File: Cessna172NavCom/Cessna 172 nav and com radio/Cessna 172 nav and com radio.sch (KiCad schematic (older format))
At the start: 19 parts, among them J1 Board connector, U1 MAX7219 COM standby, U2 COM active 4, U3 COM active 4, U4 COM active 4, U5 COM active 4, U6 COM active 4

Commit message: Minor update
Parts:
- removed R?: 27k, symbol Device:R
- removed U3, U4, U5, U6: COM active 4, Display_7Segment:KCSC02-105, symbol Display_Character:KCSC02-105
- removed U?: MAX7219 COM standby, symbol Driver_LED:MAX7219
- removed U?: COM standby 4, Display_7Segment:KCSC02-105, symbol Display_Character:KCSC02-105
- removed U?: COM standby 3, Display_7Segment:KCSC02-105, symbol Display_Character:KCSC02-105
- removed U?: COM standby 2, Display_7Segment:KCSC02-105, symbol Display_Character:KCSC02-105
- removed U?: COM standby 1, Display_7Segment:KCSC02-105, symbol Display_Character:KCSC02-105
- removed U?: COM standby 0, Display_7Segment:KCSC02-105, symbol Display_Character:KCSC02-105
- added LED2, LED3, LED4, LED5: Mobiflight digit 5, Display_7Segment:KCSC02-105, symbol Display_Character:KCSC02-105
- LED1: renamed from U2; value COM active 4 -> Mobiflight digit 5
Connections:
- net labels added: MAX0, MAX1, MAX10, MAX11, MAX12, MAX13, MAX2, MAX3, MAX4, MAX5, MAX6, MAX7, MAX9
- net labels removed: COMA_0, COMA_1, COMA_2, COMA_3, COMA_4, COMA_A, COMA_B, COMA_C, COMA_D, COMA_DP, COMA_E, COMA_F, COMA_G, COMS_0, COMS_1, COMS_2, COMS_3, COMS_4, COMS_A, COMS_B, COMS_C, COMS_D, COMS_DP, COMS_E, COMS_F, COMS_G
- wire segments 22 -> 76
- no-connect marks 17 -> 9
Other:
- note added: "5 segment display"
- note removed: "COM1 active frequency display"
- note removed: "COM1 standby frequency display"
- moved on the sheet: LED1, R1, U1

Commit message: Five digit displays wired up
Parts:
- removed LED1, LED2, LED3, LED4, LED5: Mobiflight digit 5, Display_7Segment:KCSC02-105, symbol Display_Character:KCSC02-105
- removed R1: 27k, symbol Device:R
- removed U1: MAX7219 COM standby, symbol Driver_LED:MAX7219
- C1: value C -> 10uF; footprint (none) -> Capacitor_THT:CP_Radial_D5.0mm_P2.00mm
- C2, C3, C4: value C -> 0.1uF; footprint (none) -> Capacitor_THT:C_Disc_D3.0mm_W2.0mm_P2.50mm
- J1: footprint (none) -> Connector_PinHeader_2.54mm:PinHeader_1x06_P2.54mm_Vertical
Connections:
- net labels removed: MAX0, MAX1, MAX10, MAX11, MAX12, MAX13, MAX2, MAX3, MAX4, MAX5, MAX6, MAX7, MAX9
- wire segments 76 -> 37
- no-connect marks 9 -> 2
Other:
- note added: "COMM active"
- note added: "COMM standby"
- note added: "LCD displays"
- note added: "NAV active"
- note added: "NAV standby"
- note removed: "5 segment display"

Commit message: Add rotary encoder
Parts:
- removed J1: Board connector, Connector_PinHeader_2.54mm:PinHeader_1x06_P2.54mm_Vertical, symbol Connector_Generic:Conn_02x03_Counter_Clockwise
- added C5, C6: 0.1uf, symbol Device:C
- added J1: Conn_02x08_Counter_Clockwise, symbol Connector_Generic:Conn_02x08_Counter_Clockwise
- added R5, R6, R7, R8: 10k, Resistor_SMD:R_0805_2012Metric_Pad1.15x1.40mm_HandSolder, symbol Device:R
- added SW1: Tuning encoder, Rotary_Encoder:RotaryEncoder_Alps_EC11E-Switch_Vertical_H20mm, symbol Device:Rotary_Encoder_Switch
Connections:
- net labels added: R_LEFT, R_RIGHT, SW
- wire segments 37 -> 50
- no-connect marks 2 -> 9
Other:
- note added: "Tuning rotary encoder and switch"
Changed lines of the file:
@@
 Comment4 ""
 $EndDescr
-Text GLabel 1400 1750 2    50   Input ~ 0
+Text GLabel 1400 1750 2    50   Output ~ 0
 LOAD
-Text GLabel 1400 1850 2    50   Input ~ 0
+Text GLabel 1400 1850 2    50   Output ~ 0
 CLK
-Text GLabel 1400 1950 2    50   Input ~ 0
+Text GLabel 1400 1950 2    50   Output ~ 0
 DIN
 $Comp
@@
 Wire Wire Line
 	2200 1200 2350 1200
-Text GLabel 2550 1050 2    50   Input ~ 0
+Text GLabel 2550 1050 2    50   Output ~ 0
 +5V
-Text GLabel 2550 1150 2    50   Input ~ 0
+Text GLabel 2550 1150 2    50   Output ~ 0
 GND
 $Comp
@@
 Wire Wire Line
 	2350 1200 2500 1200
-$Comp
-L Connector_Generic:Conn_02x03_Counter_Clockwise J1
-U 1 1 5F5EC70C
-P 1100 1850
-F 0 "J1" H 1150 2167 50  0000 C CNN
-F 1 "Board connector" H 1150 2076 50  0000 C CNN
-F 2 "Connector_PinHeader_2.54mm:PinHeader_1x06_P2.54mm_Vertical" H 1100 1850 50  0001 C CNN
-F 3 "~" H 1100 1850 50  0001 C CNN
-	1    1100 1850
-	1    0    0    -1
-$EndComp
-Connection ~ 900  1750
 NoConn ~ 900  1950
-Wire Notes Line
-	550  2050 2800 2050
 Wire Notes Line
 	2800 2050 2800 650
@@
 Text Notes 3200 600  0    50   ~ 0
 LCD displays
+$Comp
+L Device:Rotary_Encoder_Switch SW1
+U 1 1 5F5CDBEE
+P 4500 3550
+F 0 "SW1" H 4750 3250 50  0000 L CNN
+F 1 "Tuning encoder" H 4750 3350 50  0000 L CNN
+F 2 "Rotary_Encoder:RotaryEncoder_Alps_EC11E-Switch_Vertical_H20mm" H 4350 3710 50  0001 C CNN
+F 3 "~" H 4500 3810 50  0001 C CNN
+	1    4500 3550
+	1    0    0    -1
+$EndComp
+$Comp
+L Device:R R6
+U 1 1 5F5CE24C
+P 3750 3450
+F 0 "R6" V 3543 3450 50  0000 C CNN
+F 1 "10k" V 3634 3450 50  0000 C CNN
+F 2 "Resistor_SMD:R_0805_2012Metric_Pad1.15x1.40mm_HandSolder" V 3680 3450 50  0001 C CNN
+F 3 "~" H 3750 3450 50  0001 C CNN
+	1    3750 3450
+	0    1    1    0
+$EndComp
+$Comp
+L Device:R R7
+U 1 1 5F5CFF7A
+P 3750 3650
+F 0 "R7" V 3850 3650 50  0000 C CNN
+F 1 "10k" V 3950 3650 50  0000 C CNN
+F 2 "Resistor_SMD:R_0805_2012Metric_Pad1.15x1.40mm_HandSolder" V 3680 3650 50  0001 C CNN
+F 3 "~" H 3750 3650 50  0001 C CNN
+	1    3750 3650
+	0    1    1    0
+$EndComp
+Text GLabel 4200 3550 0    50   Input ~ 0
+GND
+Text GLabel 4800 3650 2    50   Input ~ 0
+GND
+$Comp
+L Connector_Generic:Conn_02x08_Counter_Clockwise J1
+U 1 1 5F5D3853
+P 1100 2050
+F 0 "J1" H 1150 2567 50  0000 C CNN
+F 1 "Conn_02x08_Counter_Clockwise" H 1150 2476 50  0000 C CNN
+F 2 "" H 1100 2050 50  0001 C CNN
+F 3 "~" H 1100 2050 50  0001 C CNN
+	1    1100 2050
+	1    0    0    -1
+$EndComp
+Connection ~ 900  1750
+Text GLabel 1400 2050 2    50   Input ~ 0
+SW
+Text GLabel 4800 3450 2    50   Output ~ 0
+SW
+$Comp
+L Device:C C6
+U 1 1 5F5D5010
+P 4500 4000
+F 0 "C6" V 4650 4000 50  0000 C CNN
+F 1 "0.1uf" V 4350 4000 50  0000 C CNN
+F 2 "" H 4538 3850 50  0001 C CNN
+F 3 "~" H 4500 4000 50  0001 C CNN
+	1    4500 4000
+	0    -1   -1   0
+$EndComp
+$Comp
+L Device:C C5
+U 1 1 5F5D5C2E
+P 4500 3100
+F 0 "C5" V 4350 3050 50  0000 L CNN
+F 1 "0.1uf" V 4650 3000 50  0000 L CNN
+F 2 "" H 4538 2950 50  0001 C CNN
+F 3 "~" H 4500 3100 50  0001 C CNN
+	1    4500 3100
+	0    1    1    0
+$EndComp
+Text GLabel 4650 4000 2    50   Input ~ 0
+GND
+Text GLabel 4650 3100 2    50   Input ~ 0
+GND
+Wire Wire Line
+	3900 3450 4100 3450
+Text GLabel 3450 3550 0    50   Input ~ 0
++5V
+Wire Wire Line
+	3600 3450 3600 3550
+Wire Wire Line
+	3450 3550 3600 3550
+Connection ~ 3600 3550
+Wire Wire Line
+	3600 3550 3600 3650
+Wire Wire Line
+	3900 3650 4100 3650
+$Comp
+L Device:R R8
+U 1 1 5F5DE2B1
+P 4100 4250
+F 0 "R8" H 4170 4296 50  0000 L CNN
+F 1 "10k" H 4170 4205 50  0000 L CNN
+F 2 "Resistor_SMD:R_0805_2012Metric_Pad1.15x1.40mm_HandSolder" V 4030 4250 50  0001 C CNN
+F 3 "~" H 4100 4250 50  0001 C CNN
+	1    4100 4250
+	1    0    0    -1
+$EndComp
+Wire Wire Line
+	4100 4100 4100 4000
+Connection ~ 4100 3650
+Wire Wire Line
+	4100 3650 4200 3650
+Wire Wire Line
+	4350 4000 4100 4000
+Connection ~ 4100 4000
+Wire Wire Line
+	4100 4000 4100 3650
+Text GLabel 4100 4400 3    50   Output ~ 0
+R_LEFT
+Wire Wire Line
+	4100 3450 4100 3100
+Wire Wire Line
+	4100 3100 4350 3100
+Connection ~ 4100 3450
+Wire Wire Line
+	4100 3450 4200 3450
+$Comp
+L Device:R R5
+U 1 1 5F5E3E59
+P 4100 2850
+F 0 "R5" H 4170 2896 50  0000 L CNN
+F 1 "10k" H 4170 2805 50  0000 L CNN
+F 2 "Resistor_SMD:R_0805_2012Metric_Pad1.15x1.40mm_HandSolder" V 4030 2850 50  0001 C CNN
+F 3 "~" H 4100 2850 50  0001 C CNN
+	1    4100 2850
+	1    0    0    -1
+$EndComp
+Wire Wire Line
+	4100 3000 4100 3100
+Connection ~ 4100 3100
+Text GLabel 4100 2700 1    50   Output ~ 0
+R_RIGHT
+Text GLabel 1400 2150 2    50   Input ~ 0
+R_LEFT
+Text GLabel 1400 2250 2    50   Input ~ 0
+R_RIGHT
+NoConn ~ 900  2050
+NoConn ~ 900  2150
+NoConn ~ 900  2250
+NoConn ~ 900  2350
+NoConn ~ 900  2450
+NoConn ~ 1400 2450
+NoConn ~ 1400 2350
+Wire Notes Line
+	5450 2300 5450 4750
+Wire Notes Line
+	5450 4750 3200 4750
+Wire Notes Line
+	3200 4750 3200 2300
+Wire Notes Line
+	3200 2300 5450 2300
+Text Notes 3200 2250 0    50   ~ 0
+Tuning rotary encoder and switch
 $EndSCHEMATC

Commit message: 3D model for LED
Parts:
- C5, C6: footprint (none) -> Capacitor_THT:C_Disc_D3.0mm_W2.0mm_P2.50mm
- J1: footprint (none) -> Connector_PinHeader_2.54mm:PinHeader_1x16_P2.54mm_Vertical
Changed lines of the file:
@@
 F 0 "J1" H 1150 2567 50  0000 C CNN
 F 1 "Conn_02x08_Counter_Clockwise" H 1150 2476 50  0000 C CNN
-F 2 "" H 1100 2050 50  0001 C CNN
+F 2 "Connector_PinHeader_2.54mm:PinHeader_1x16_P2.54mm_Vertical" H 1100 2050 50  0001 C CNN
 F 3 "~" H 1100 2050 50  0001 C CNN
 	1    1100 2050
@@
 F 0 "C6" V 4650 4000 50  0000 C CNN
 F 1 "0.1uf" V 4350 4000 50  0000 C CNN
-F 2 "" H 4538 3850 50  0001 C CNN
+F 2 "Capacitor_THT:C_Disc_D3.0mm_W2.0mm_P2.50mm" H 4538 3850 50  0001 C CNN
 F 3 "~" H 4500 4000 50  0001 C CNN
 	1    4500 4000
@@
 F 0 "C5" V 4350 3050 50  0000 L CNN
 F 1 "0.1uf" V 4650 3000 50  0000 L CNN
-F 2 "" H 4538 2950 50  0001 C CNN
+F 2 "Capacitor_THT:C_Disc_D3.0mm_W2.0mm_P2.50mm" H 4538 2950 50  0001 C CNN
 F 3 "~" H 4500 3100 50  0001 C CNN
 	1    4500 3100

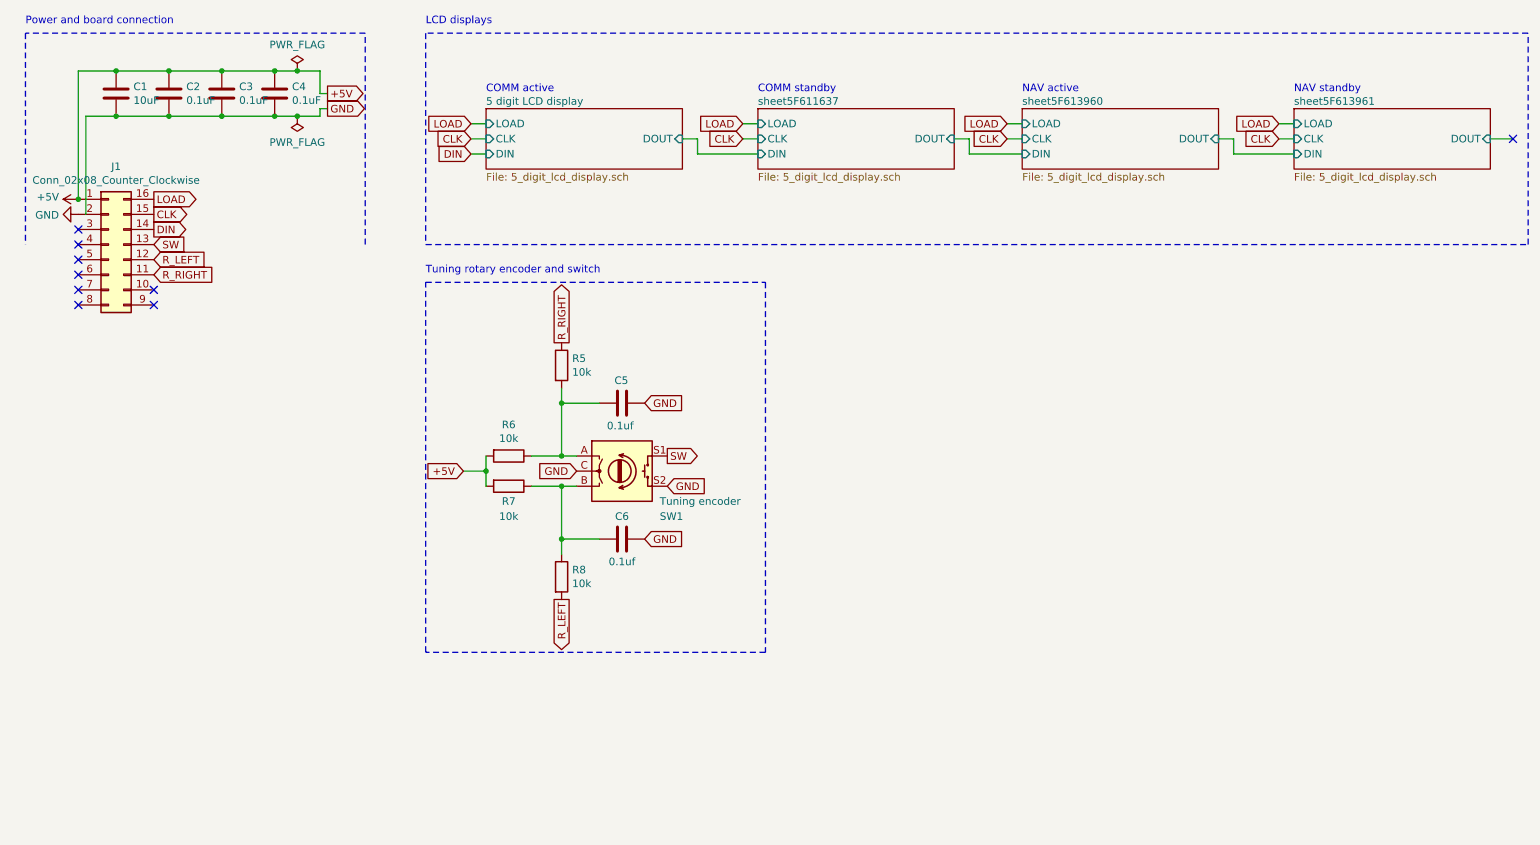
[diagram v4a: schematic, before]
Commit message: Updated schematic to include remaining items.
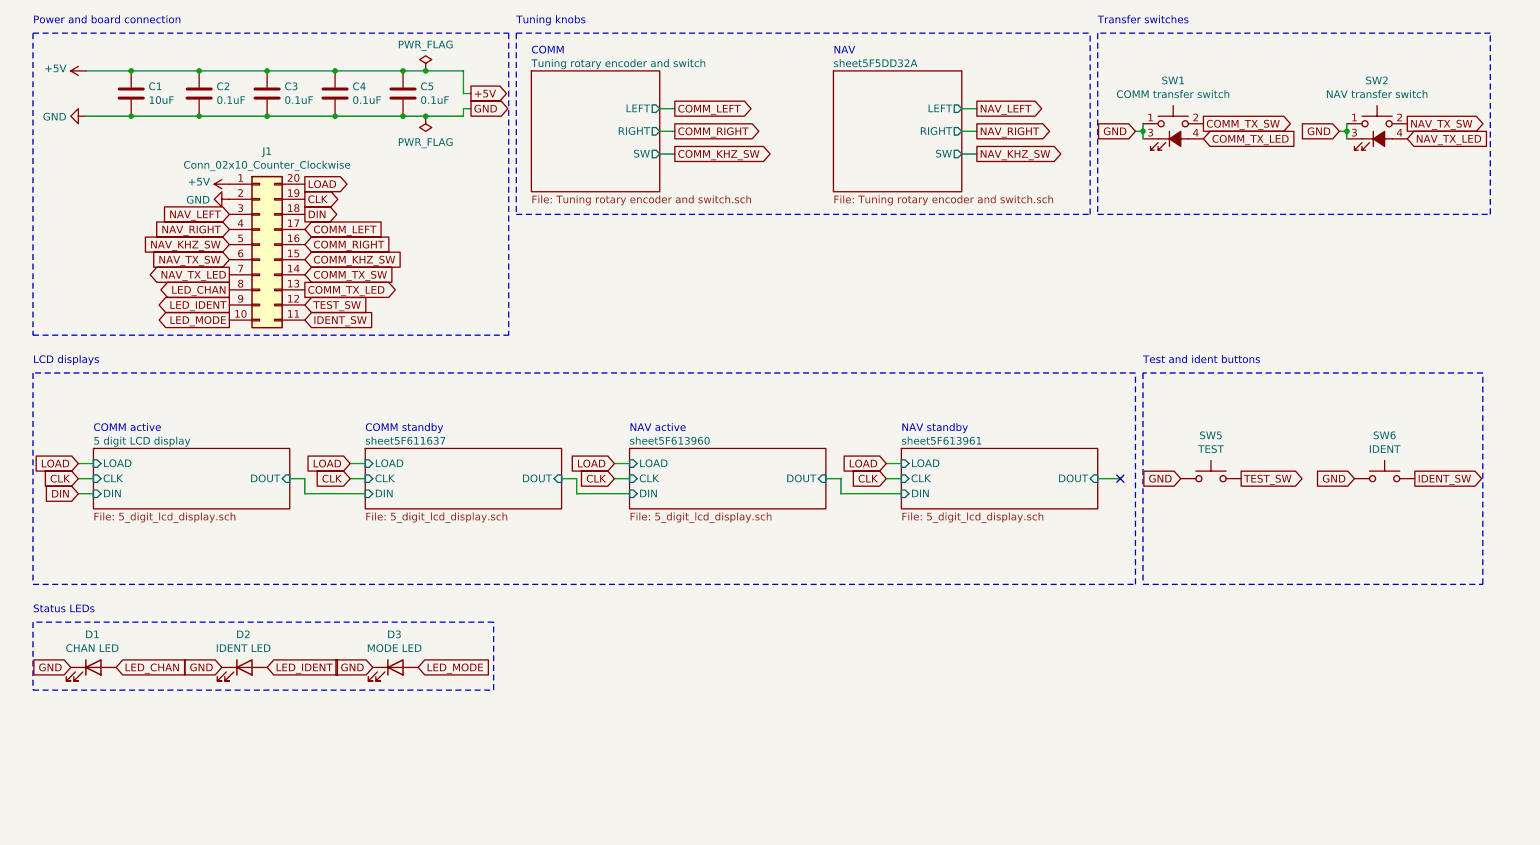
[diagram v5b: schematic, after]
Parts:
- removed C5, C6: 0.1uf, Capacitor_THT:C_Disc_D3.0mm_W2.0mm_P2.50mm, symbol Device:C
- removed J1: Conn_02x08_Counter_Clockwise, Connector_PinHeader_2.54mm:PinHeader_1x16_P2.54mm_Vertical, symbol Connector_Generic:Conn_02x08_Counter_Clockwise
- removed R5, R6, R7, R8: 10k, Resistor_SMD:R_0805_2012Metric_Pad1.15x1.40mm_HandSolder, symbol Device:R
- removed SW1: Tuning encoder, Rotary_Encoder:RotaryEncoder_Alps_EC11E-Switch_Vertical_H20mm, symbol Device:Rotary_Encoder_Switch
- added C3: 0.1uF, Capacitor_THT:C_Disc_D3.0mm_W2.0mm_P2.50mm, symbol Device:C
- added D1: CHAN LED, LED_THT:LED_D5.0mm, symbol Device:LED
- added D2: IDENT LED, LED_THT:LED_D5.0mm, symbol Device:LED
- added D3: MODE LED, LED_THT:LED_D5.0mm, symbol Device:LED
- added J1: Conn_02x10_Counter_Clockwise, Connector_PinHeader_2.54mm:PinHeader_2x10_P2.54mm_Horizontal, symbol Connector_Generic:Conn_02x10_Counter_Clockwise
- added SW1: COMM transfer switch, Button_Switch_THT:SW_TH_Tactile_Omron_B3F-10xx, symbol Switch:SW_Push_LED
- added SW2: NAV transfer switch, Button_Switch_THT:SW_TH_Tactile_Omron_B3F-10xx, symbol Switch:SW_Push_LED
- added SW5: TEST, Button_Switch_THT:SW_PUSH_6mm, symbol Switch:SW_Push
- added SW6: IDENT, Button_Switch_THT:SW_PUSH_6mm, symbol Switch:SW_Push
- renumbered C3 to C4, C4 to C5
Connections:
- net +5V: now also C3.1, J1.1 (Pin_1)
- net CLK: now also J1.19 (Pin_19)
- net DIN: now also J1.18 (Pin_18)
- net GND: now also C3.2, D1.1 (K), D2.1 (K), D3.1 (K), J1.2 (Pin_2), SW1.1, SW1.3 (K), SW2.1, SW2.3 (K), SW5.1, SW6.1
- net LOAD: now also J1.20 (Pin_20)
- new net COMM_KHZ_SW: J1.15 (Pin_15)
- new net COMM_LEFT: J1.17 (Pin_17)
- new net COMM_RIGHT: J1.16 (Pin_16)
- new net COMM_TX_LED: J1.13 (Pin_13), SW1.4 (A)
- new net COMM_TX_SW: J1.14 (Pin_14), SW1.2
- new net IDENT_SW: J1.11 (Pin_11), SW6.2
- new net LED_CHAN: D1.2 (A), J1.8 (Pin_8)
- new net LED_IDENT: D2.2 (A), J1.9 (Pin_9)
- new net LED_MODE: D3.2 (A), J1.10 (Pin_10)
- new net NAV_KHZ_SW: J1.5 (Pin_5)
- new net NAV_LEFT: J1.3 (Pin_3)
- new net NAV_RIGHT: J1.4 (Pin_4)
- new net NAV_TX_LED: J1.7 (Pin_7), SW2.4 (A)
- new net NAV_TX_SW: J1.6 (Pin_6), SW2.2
- new net TEST_SW: J1.12 (Pin_12), SW5.2
- no-connect marks 9 -> 1
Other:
- note added: "COMM"
- note added: "NAV"
- note added: "Status LEDs"
- note added: "Test and ident buttons"
- note added: "Transfer switches"
- note added: "Tuning knobs"
- note removed: "Tuning rotary encoder and switch"
- moved on the sheet: C1, C2, C4, C5

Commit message: Proper LED buttons and switches
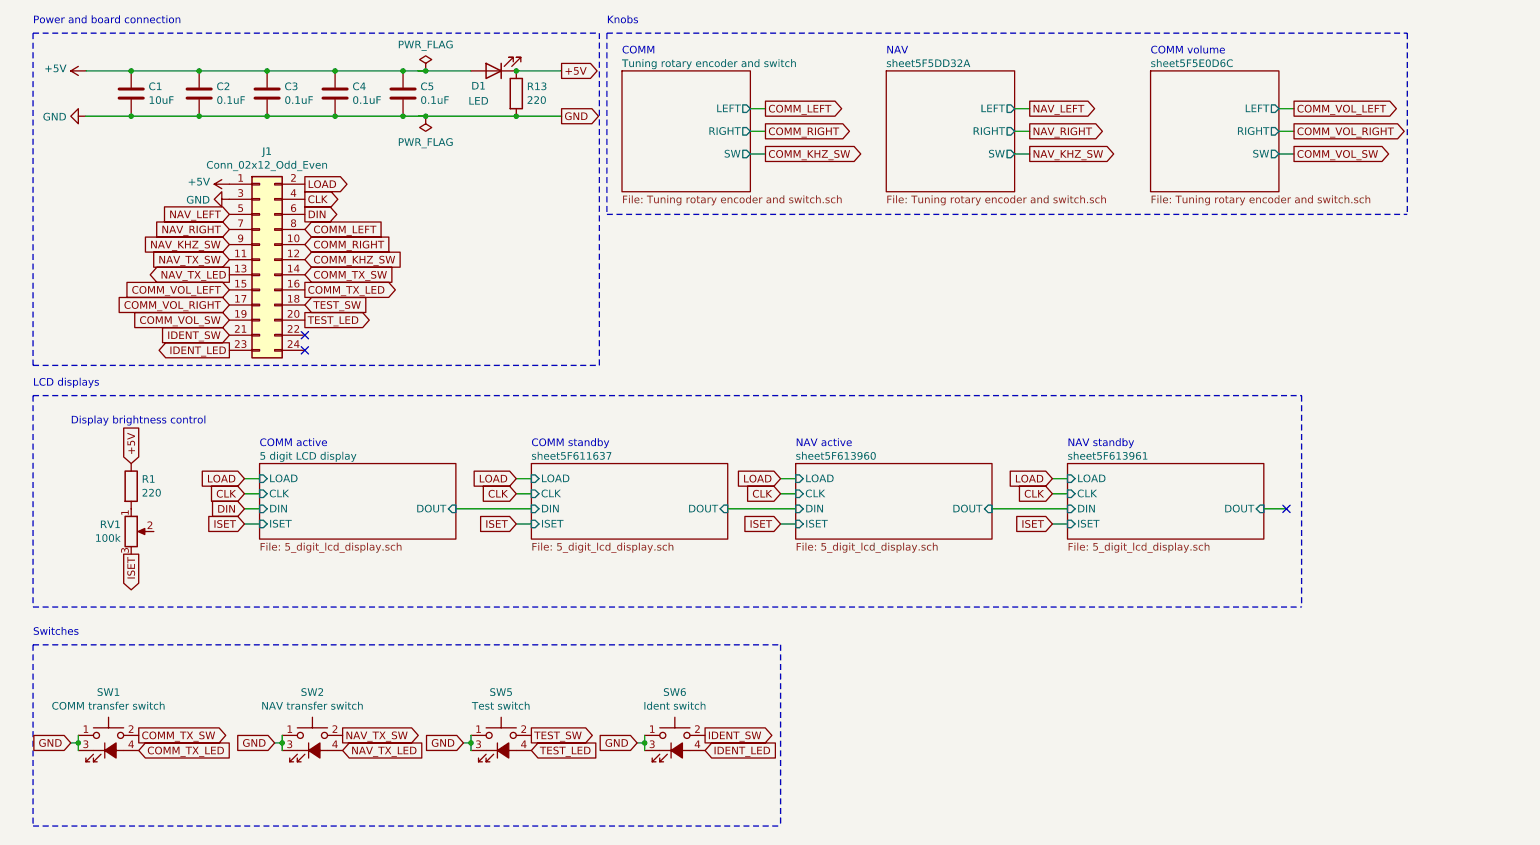
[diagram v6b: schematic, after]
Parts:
- removed D2: IDENT LED, LED_THT:LED_D5.0mm, symbol Device:LED
- removed D3: MODE LED, LED_THT:LED_D5.0mm, symbol Device:LED
- removed J1: Conn_02x10_Counter_Clockwise, Connector_PinHeader_2.54mm:PinHeader_2x10_P2.54mm_Horizontal, symbol Connector_Generic:Conn_02x10_Counter_Clockwise
- removed SW5: TEST, Button_Switch_THT:SW_PUSH_6mm, symbol Switch:SW_Push
- removed SW6: IDENT, Button_Switch_THT:SW_PUSH_6mm, symbol Switch:SW_Push
- added J1: Conn_02x12_Odd_Even, Connector_PinHeader_2.54mm:PinHeader_2x12_P2.54mm_Vertical, symbol Connector_Generic:Conn_02x12_Odd_Even
- added R1, R13: 220, Resistor_SMD:R_0805_2012Metric_Pad1.15x1.40mm_HandSolder, symbol Device:R
- added RV1: 100k, Potentiometer_THT:Potentiometer_Piher_PT-10-V10_Vertical_Hole, symbol Device:R_POT
- added SW5: Test switch, Button_Switch_THT:SW_TH_Tactile_Omron_B3F-10xx, symbol Switch:SW_Push_LED
- added SW6: Ident switch, Button_Switch_THT:SW_TH_Tactile_Omron_B3F-10xx, symbol Switch:SW_Push_LED
- C2, C3, C4, C5: footprint Capacitor_THT:C_Disc_D3.0mm_W2.0mm_P2.50mm -> Capacitor_SMD:C_0805_2012Metric_Pad1.15x1.40mm_HandSolder
- D1: value CHAN LED -> LED; footprint LED_THT:LED_D5.0mm -> LED_SMD:LED_0805_2012Metric_Pad1.15x1.40mm_HandSolder
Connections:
- net labels added: COMM_VOL_LEFT, COMM_VOL_RIGHT, COMM_VOL_SW, IDENT_LED, ISET, TEST_LED
- net labels removed: LED_CHAN, LED_IDENT, LED_MODE
- wire segments 49 -> 56
- no-connect marks 1 -> 3
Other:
- note added: "COMM volume"
- note added: "Display brightness control"
- note added: "Knobs"
- note added: "Switches"
- note removed: "Status LEDs"
- note removed: "Test and ident buttons"
- note removed: "Transfer switches"
- note removed: "Tuning knobs"
